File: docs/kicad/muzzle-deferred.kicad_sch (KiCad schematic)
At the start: 0 parts

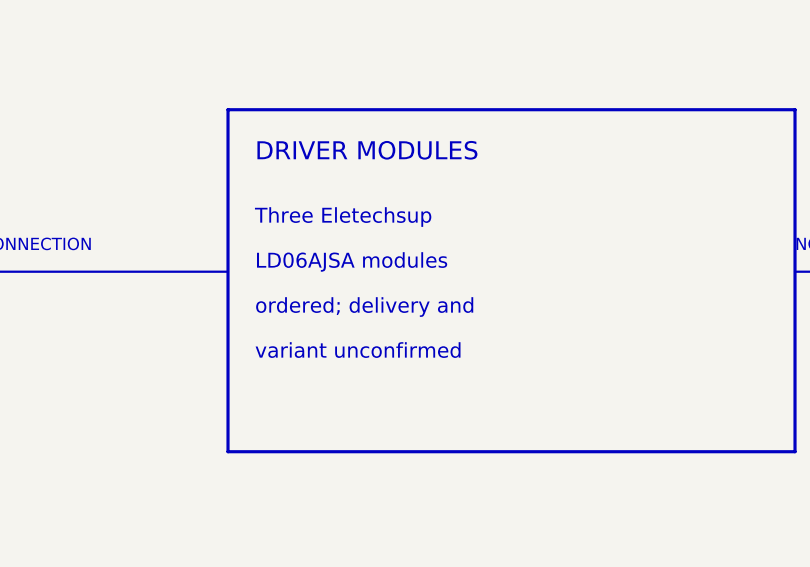
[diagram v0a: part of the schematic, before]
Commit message: docs: remove hardware procurement status
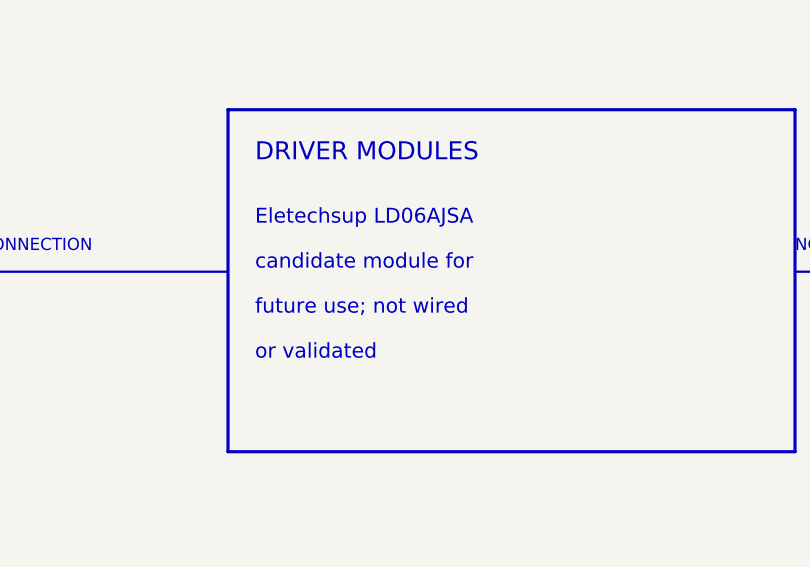
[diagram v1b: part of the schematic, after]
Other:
- note added: "Eletechsup LD06AJSA"
- note added: "candidate module for"
- note added: "future use; not wired"
- note added: "or validated"
- note removed: "LD06AJSA modules"
- note removed: "Three Eletechsup"
- note removed: "ordered; delivery and"
- note removed: "variant unconfirmed"
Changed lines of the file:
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@@
   (polyline (pts (xy 120 55) (xy 183 55) (xy 183 93) (xy 120 93) (xy 120 55)) (stroke (width 0.35) (type default)) (fill (type none)))
   (text "DRIVER MODULES" (at 123 61 0) (effects (font (size 2.0 2.0)) (justify left bottom)))
-  (text "Three Eletechsup" (at 123 68 0) (effects (font (size 1.65 1.65)) (justify left bottom)))
-  (text "LD06AJSA modules" (at 123 73 0) (effects (font (size 1.65 1.65)) (justify left bottom)))
-  (text "ordered; delivery and" (at 123 78 0) (effects (font (size 1.65 1.65)) (justify left bottom)))
-  (text "variant unconfirmed" (at 123 83 0) (effects (font (size 1.65 1.65)) (justify left bottom)))
+  (text "Eletechsup LD06AJSA" (at 123 68 0) (effects (font (size 1.65 1.65)) (justify left bottom)))
+  (text "candidate module for" (at 123 73 0) (effects (font (size 1.65 1.65)) (justify left bottom)))
+  (text "future use; not wired" (at 123 78 0) (effects (font (size 1.65 1.65)) (justify left bottom)))
+  (text "or validated" (at 123 83 0) (effects (font (size 1.65 1.65)) (justify left bottom)))
   (polyline (pts (xy 214 55) (xy 277 55) (xy 277 93) (xy 214 93) (xy 214 55)) (stroke (width 0.35) (type default)) (fill (type none)))
   (text "COOL-WHITE LED" (at 217 61 0) (effects (font (size 2.0 2.0)) (justify left bottom)))
